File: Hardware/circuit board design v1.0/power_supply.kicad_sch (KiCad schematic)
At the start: 0 parts

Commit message: power management schematic done
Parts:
- added C? (x2): C_Small, symbol Device:C_Small
- added D?: DFLS130L, symbol Components:DFLS130L
- added J?: USB_B_Micro, symbol Connector:USB_B_Micro
- added J?: Conn_01x02_Male, symbol Connector:Conn_01x02_Male
- added R? (x2): R, symbol Device:R
- added U?: NCP161ASN180T1G, Components:SOT95P280X145-5N, symbol Components:NCP161ASN180T1G
- added U?: STF202-22T1G, Components:STF202-22T1G, symbol Components:STF202-22T1G
- added U?: MAX40203_SOT23, Package_TO_SOT_SMD:SOT-23-5, symbol Components:MAX40203_SOT23
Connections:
- new net: C?.1, D?.1 (K), U?.1 (IN), U?.3 (EN), U?.5 (OUT)
- new net: J?.2 (D-), U?.5
- new net: J?.3 (D+), U?.4
- new net: J?.1 (Pin_1), R?.1, U?.1 (VDD), U?.3 (EN)
- new net +3.3V: C?.1, U?.5 (OUT)
- new net GND: C?.2, C?.2, J?.2 (Pin_2), J?.5 (GND), J?.6 (Shield), R?.2, U?.2 (GND), U?.2 (GND), U?.6
- new net PWR_BVOLTS: R?.1, R?.2
- new net VBUS: D?.2 (A), J?.1 (VBUS), U?.1
- new net usb_db: U?.3
- new net usb_dm: U?.2
- no-connect marks 0 -> 1

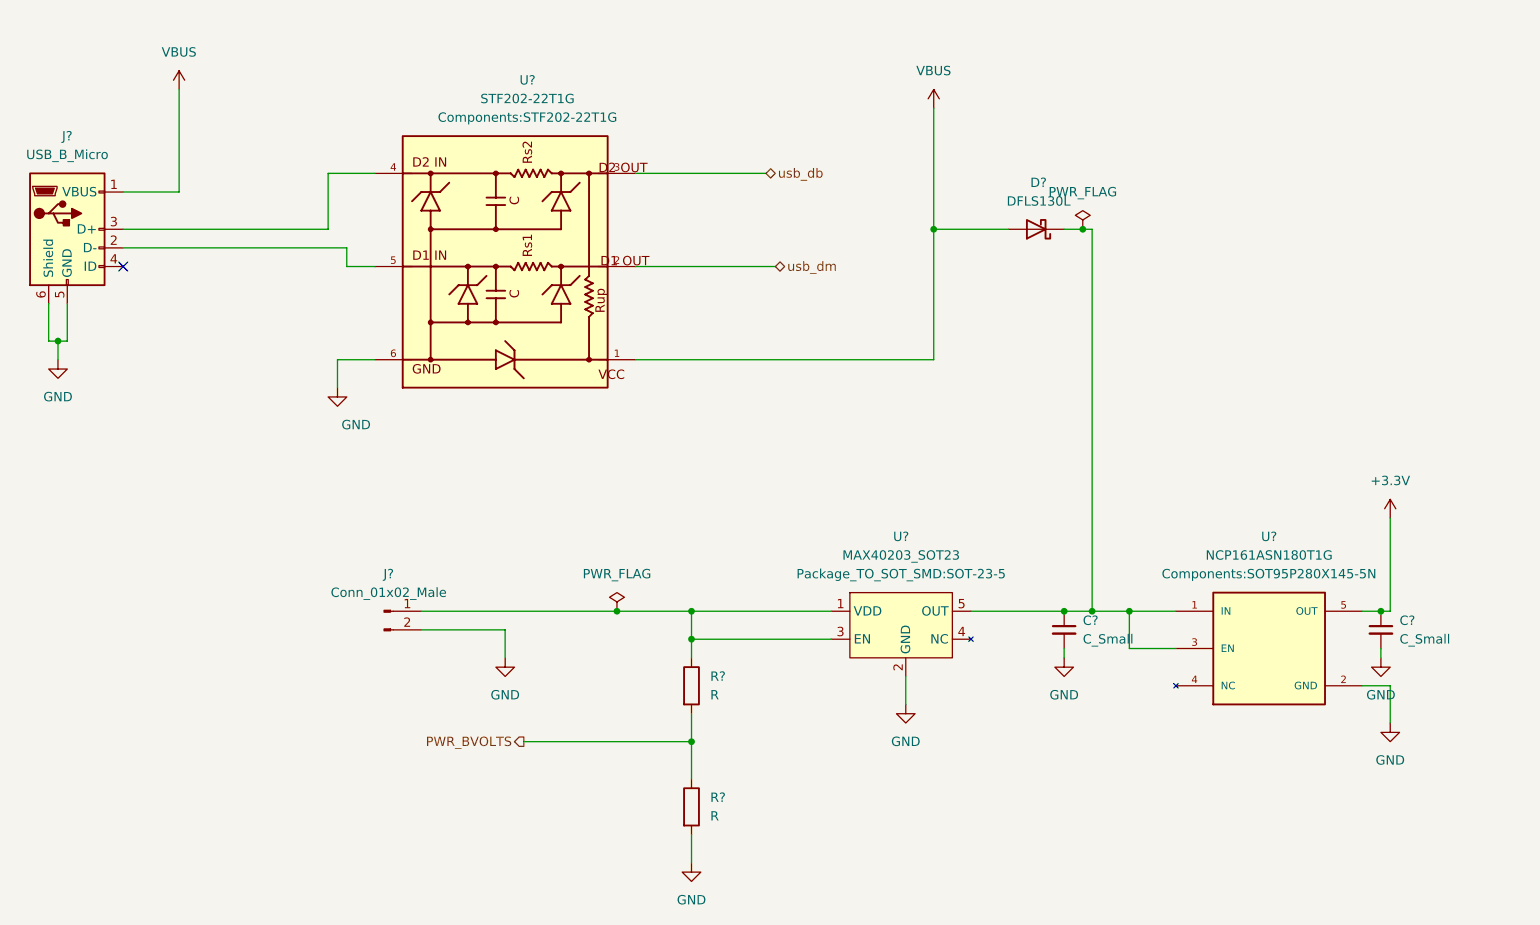
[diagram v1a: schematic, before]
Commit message: BMI088 schematic
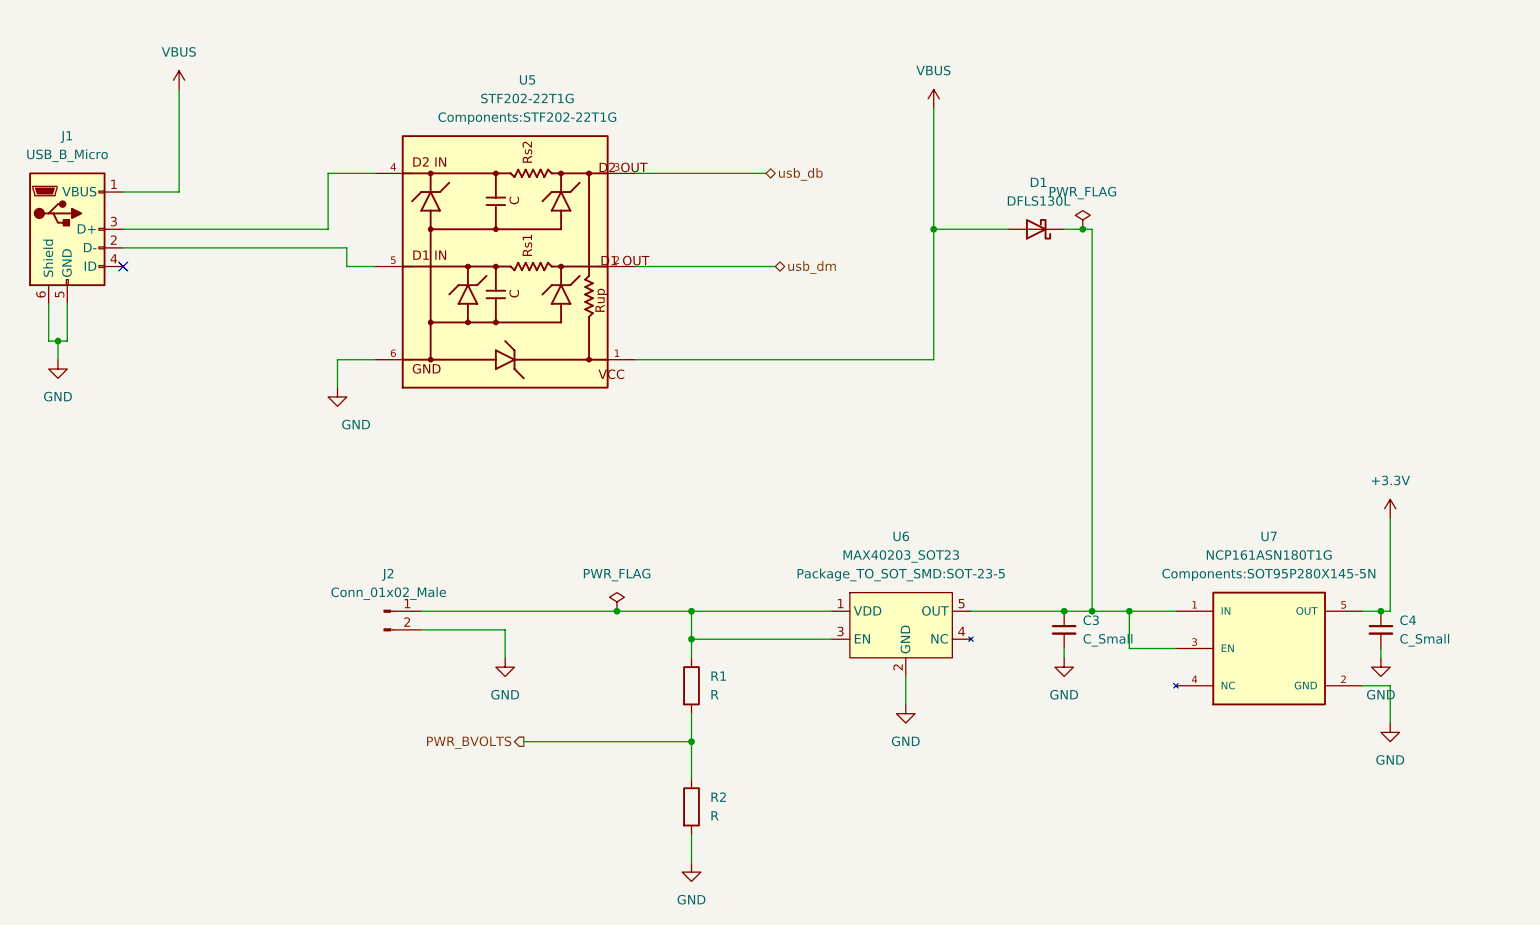
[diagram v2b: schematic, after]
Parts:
- gave numbers to parts that had none: 10
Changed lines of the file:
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@@
   (symbol (lib_id "power:VBUS") (at 166.37 31.75 0) (unit 1)
     (in_bom yes) (on_board yes) (fields_autoplaced)
-    (property "Reference" "#PWR?" (id 0) (at 166.37 35.56 0)
+    (property "Reference" "#PWR0105" (id 0) (at 166.37 35.56 0)
       (effects (font (size 1.27 1.27)) hide)
     )
@@
   (symbol (lib_id "power:+3.3V") (at 228.6 87.63 0) (unit 1)
     (in_bom yes) (on_board yes) (fields_autoplaced)
-    (property "Reference" "#PWR?" (id 0) (at 228.6 91.44 0)
+    (property "Reference" "#PWR0114" (id 0) (at 228.6 91.44 0)
       (effects (font (size 1.27 1.27)) hide)
     )
@@
   (symbol (lib_id "power:GND") (at 227.33 106.68 0) (unit 1)
     (in_bom yes) (on_board yes) (fields_autoplaced)
-    (property "Reference" "#PWR?" (id 0) (at 227.33 113.03 0)
+    (property "Reference" "#PWR0112" (id 0) (at 227.33 113.03 0)
       (effects (font (size 1.27 1.27)) hide)
     )
@@
   (symbol (lib_id "power:GND") (at 107.95 106.68 0) (unit 1)
     (in_bom yes) (on_board yes) (fields_autoplaced)
-    (property "Reference" "#PWR?" (id 0) (at 107.95 113.03 0)
+    (property "Reference" "#PWR0108" (id 0) (at 107.95 113.03 0)
       (effects (font (size 1.27 1.27)) hide)
     )
@@
   (symbol (lib_id "Components:NCP161ASN180T1G") (at 212.09 105.41 0) (unit 1)
     (in_bom yes) (on_board yes) (fields_autoplaced)
-    (property "Reference" "U?" (id 0) (at 212.09 90.17 0))
+    (property "Reference" "U7" (id 0) (at 212.09 90.17 0))
     (property "Value" "NCP161ASN180T1G" (id 1) (at 212.09 92.71 0))
     (property "Footprint" "Components:SOT95P280X145-5N" (id 2) (at 212.09 95.25 0))
@@
   (symbol (lib_id "power:GND") (at 184.15 106.68 0) (unit 1)
     (in_bom yes) (on_board yes) (fields_autoplaced)
-    (property "Reference" "#PWR?" (id 0) (at 184.15 113.03 0)
+    (property "Reference" "#PWR0113" (id 0) (at 184.15 113.03 0)
       (effects (font (size 1.27 1.27)) hide)
     )
@@
   (symbol (lib_id "Device:C_Small") (at 227.33 102.87 0) (unit 1)
     (in_bom yes) (on_board yes) (fields_autoplaced)
-    (property "Reference" "C?" (id 0) (at 229.87 101.6062 0)
+    (property "Reference" "C4" (id 0) (at 229.87 101.6062 0)
       (effects (font (size 1.27 1.27)) (justify left))
     )
@@
   (symbol (lib_id "Connector:USB_B_Micro") (at 48.26 48.26 0) (unit 1)
     (in_bom yes) (on_board yes) (fields_autoplaced)
-    (property "Reference" "J?" (id 0) (at 48.26 35.56 0))
+    (property "Reference" "J1" (id 0) (at 48.26 35.56 0))
     (property "Value" "USB_B_Micro" (id 1) (at 48.26 38.1 0))
     (property "Footprint" "" (id 2) (at 52.07 49.53 0)
@@
   (symbol (lib_id "power:GND") (at 85.09 69.85 0) (unit 1)
     (in_bom yes) (on_board yes)
-    (property "Reference" "#PWR?" (id 0) (at 85.09 76.2 0)
+    (property "Reference" "#PWR0109" (id 0) (at 85.09 76.2 0)
       (effects (font (size 1.27 1.27)) hide)
     )
@@
   (symbol (lib_id "power:GND") (at 133.35 134.62 0) (unit 1)
     (in_bom yes) (on_board yes) (fields_autoplaced)
-    (property "Reference" "#PWR?" (id 0) (at 133.35 140.97 0)
+    (property "Reference" "#PWR0110" (id 0) (at 133.35 140.97 0)
       (effects (font (size 1.27 1.27)) hide)
     )
@@
   (symbol (lib_id "Device:R") (at 133.35 127 0) (unit 1)
     (in_bom yes) (on_board yes)
-    (property "Reference" "R?" (id 0) (at 135.89 125.7299 0)
+    (property "Reference" "R2" (id 0) (at 135.89 125.7299 0)
       (effects (font (size 1.27 1.27)) (justify left))
     )
@@
   (symbol (lib_id "power:PWR_FLAG") (at 123.19 100.33 0) (unit 1)
     (in_bom yes) (on_board yes) (fields_autoplaced)
-    (property "Reference" "#FLG?" (id 0) (at 123.19 98.425 0)
+    (property "Reference" "#FLG0101" (id 0) (at 123.19 98.425 0)
       (effects (font (size 1.27 1.27)) hide)
     )
@@
   (symbol (lib_id "Components:STF202-22T1G") (at 107.95 53.34 0) (unit 1)
     (in_bom yes) (on_board yes) (fields_autoplaced)
-    (property "Reference" "U?" (id 0) (at 110.9957 27.94 0))
+    (property "Reference" "U5" (id 0) (at 110.9957 27.94 0))
     (property "Value" "STF202-22T1G" (id 1) (at 110.9957 30.48 0))
     (property "Footprint" "Components:STF202-22T1G" (id 2) (at 110.9957 33.02 0))
@@
   (symbol (lib_id "power:GND") (at 228.6 115.57 0) (unit 1)
     (in_bom yes) (on_board yes) (fields_autoplaced)
-    (property "Reference" "#PWR?" (id 0) (at 228.6 121.92 0)
+    (property "Reference" "#PWR0111" (id 0) (at 228.6 121.92 0)
       (effects (font (size 1.27 1.27)) hide)
     )
@@
   (symbol (lib_id "power:GND") (at 162.56 113.03 0) (unit 1)
     (in_bom yes) (on_board yes) (fields_autoplaced)
-    (property "Reference" "#PWR?" (id 0) (at 162.56 119.38 0)
+    (property "Reference" "#PWR0115" (id 0) (at 162.56 119.38 0)
       (effects (font (size 1.27 1.27)) hide)
     )
@@
   (symbol (lib_id "Components:MAX40203_SOT23") (at 161.29 101.6 0) (unit 1)
     (in_bom yes) (on_board yes) (fields_autoplaced)
-    (property "Reference" "U?" (id 0) (at 161.925 90.17 0))
+    (property "Reference" "U6" (id 0) (at 161.925 90.17 0))
     (property "Value" "MAX40203_SOT23" (id 1) (at 161.925 92.71 0))
     (property "Footprint" "Package_TO_SOT_SMD:SOT-23-5" (id 2) (at 161.925 95.25 0))
@@
   (symbol (lib_id "power:GND") (at 46.99 66.04 0) (unit 1)
     (in_bom yes) (on_board yes) (fields_autoplaced)
-    (property "Reference" "#PWR?" (id 0) (at 46.99 72.39 0)
+    (property "Reference" "#PWR0107" (id 0) (at 46.99 72.39 0)
       (effects (font (size 1.27 1.27)) hide)
     )
@@
   (symbol (lib_id "Components:DFLS130L") (at 180.34 48.26 180) (unit 1)
     (in_bom yes) (on_board yes) (fields_autoplaced)
-    (property "Reference" "D?" (id 0) (at 180.6575 41.91 0))
+    (property "Reference" "D1" (id 0) (at 180.6575 41.91 0))
     (property "Value" "DFLS130L" (id 1) (at 180.6575 44.45 0))
     (property "Footprint" "" (id 2) (at 180.34 48.26 0)
@@
   (symbol (lib_id "power:PWR_FLAG") (at 186.69 48.26 0) (unit 1)
     (in_bom yes) (on_board yes) (fields_autoplaced)
-    (property "Reference" "#FLG?" (id 0) (at 186.69 46.355 0)
+    (property "Reference" "#FLG0102" (id 0) (at 186.69 46.355 0)
       (effects (font (size 1.27 1.27)) hide)
     )
@@
   (symbol (lib_id "power:VBUS") (at 63.5 29.21 0) (unit 1)
     (in_bom yes) (on_board yes) (fields_autoplaced)
-    (property "Reference" "#PWR?" (id 0) (at 63.5 33.02 0)
+    (property "Reference" "#PWR0106" (id 0) (at 63.5 33.02 0)
       (effects (font (size 1.27 1.27)) hide)
     )
@@
   (symbol (lib_id "Device:R") (at 133.35 110.49 0) (unit 1)
     (in_bom yes) (on_board yes) (fields_autoplaced)
-    (property "Reference" "R?" (id 0) (at 135.89 109.2199 0)
+    (property "Reference" "R1" (id 0) (at 135.89 109.2199 0)
       (effects (font (size 1.27 1.27)) (justify left))
     )
@@
   (symbol (lib_id "Device:C_Small") (at 184.15 102.87 0) (unit 1)
     (in_bom yes) (on_board yes) (fields_autoplaced)
-    (property "Reference" "C?" (id 0) (at 186.69 101.6062 0)
+    (property "Reference" "C3" (id 0) (at 186.69 101.6062 0)
       (effects (font (size 1.27 1.27)) (justify left))
     )
@@
   (symbol (lib_id "Connector:Conn_01x02_Male") (at 91.44 100.33 0) (unit 1)
     (in_bom yes) (on_board yes) (fields_autoplaced)
-    (property "Reference" "J?" (id 0) (at 92.075 95.25 0))
+    (property "Reference" "J2" (id 0) (at 92.075 95.25 0))
     (property "Value" "Conn_01x02_Male" (id 1) (at 92.075 97.79 0))
     (property "Footprint" "" (id 2) (at 91.44 100.33 0)

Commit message: Created stm32mx project and started on layout
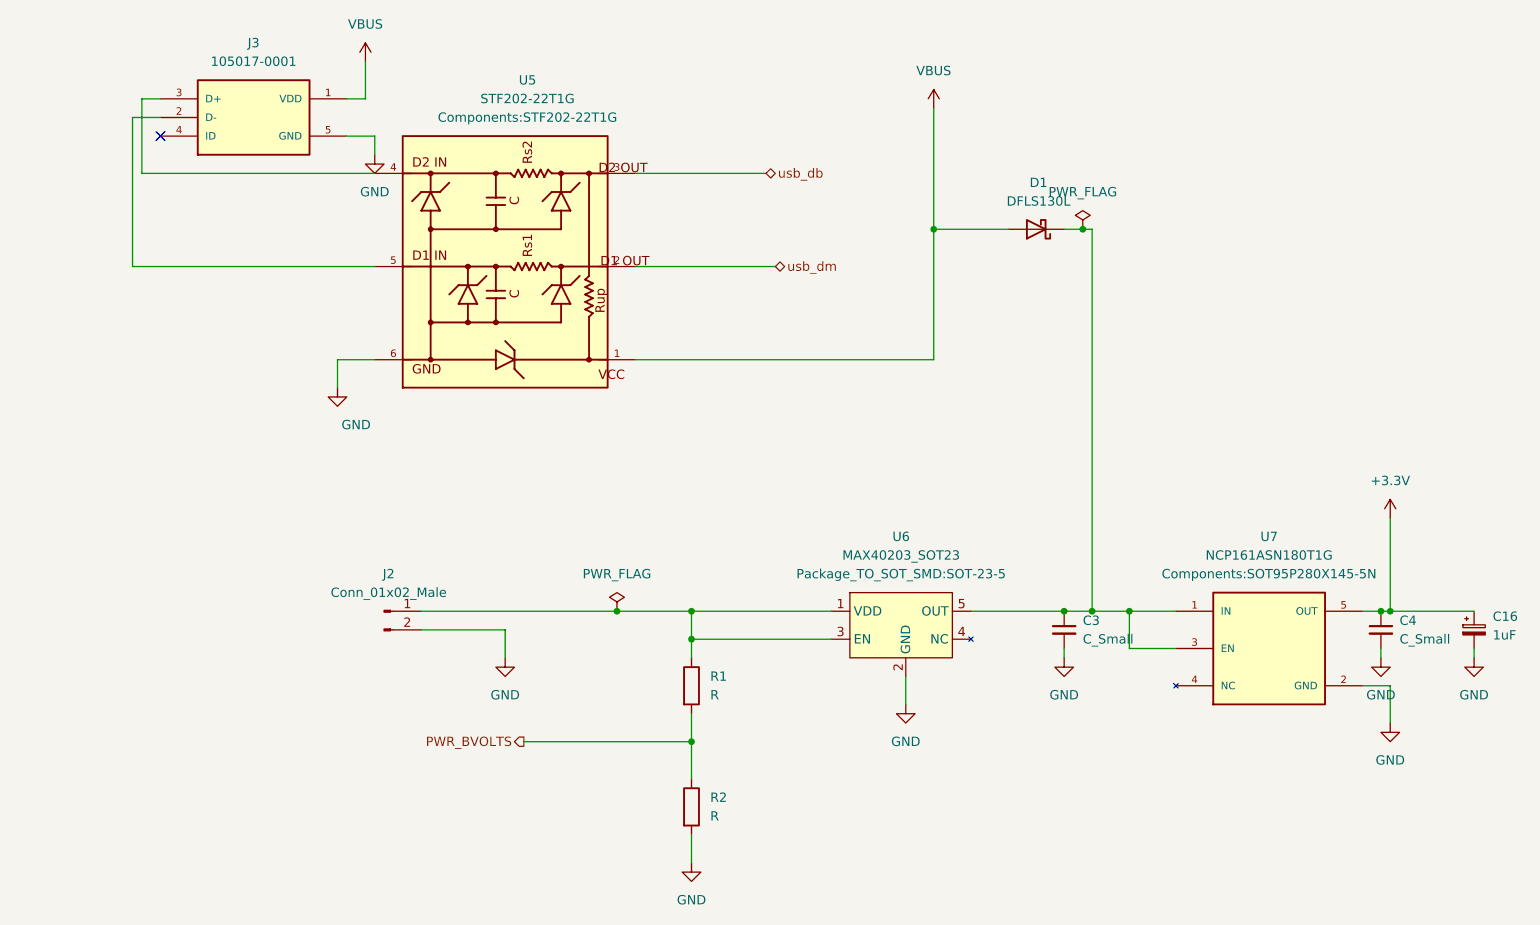
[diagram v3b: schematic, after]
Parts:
- removed J1: USB_B_Micro, symbol Connector:USB_B_Micro
- added C16: 1uF, Capacitor_SMD:C_1206_3216Metric, symbol Device:C_Polarized_Small
- added J3: 105017-0001, MOLEX_105017-0001, symbol Components:105017-0001
- C3, C4, R1, R2: footprint (none) -> Capacitor_SMD:C_0603_1608Metric
- D1: footprint (none) -> Components:PowerDI123
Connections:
- net +3.3V: now also C16.1
- net GND: now also C16.2, J3.5 (GND)
- net VBUS: now also J3.1 (VDD)
- net at U5.5: now also J3.2 (D-)
- net at U5.4: now also J3.3 (D+)
